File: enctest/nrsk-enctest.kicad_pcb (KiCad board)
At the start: 2 copper layers, 69.6 x 32 mm, 10 parts, among them J1 RP2040-Zero left, J2 RP2040-Zero right, SW1 Layer 1

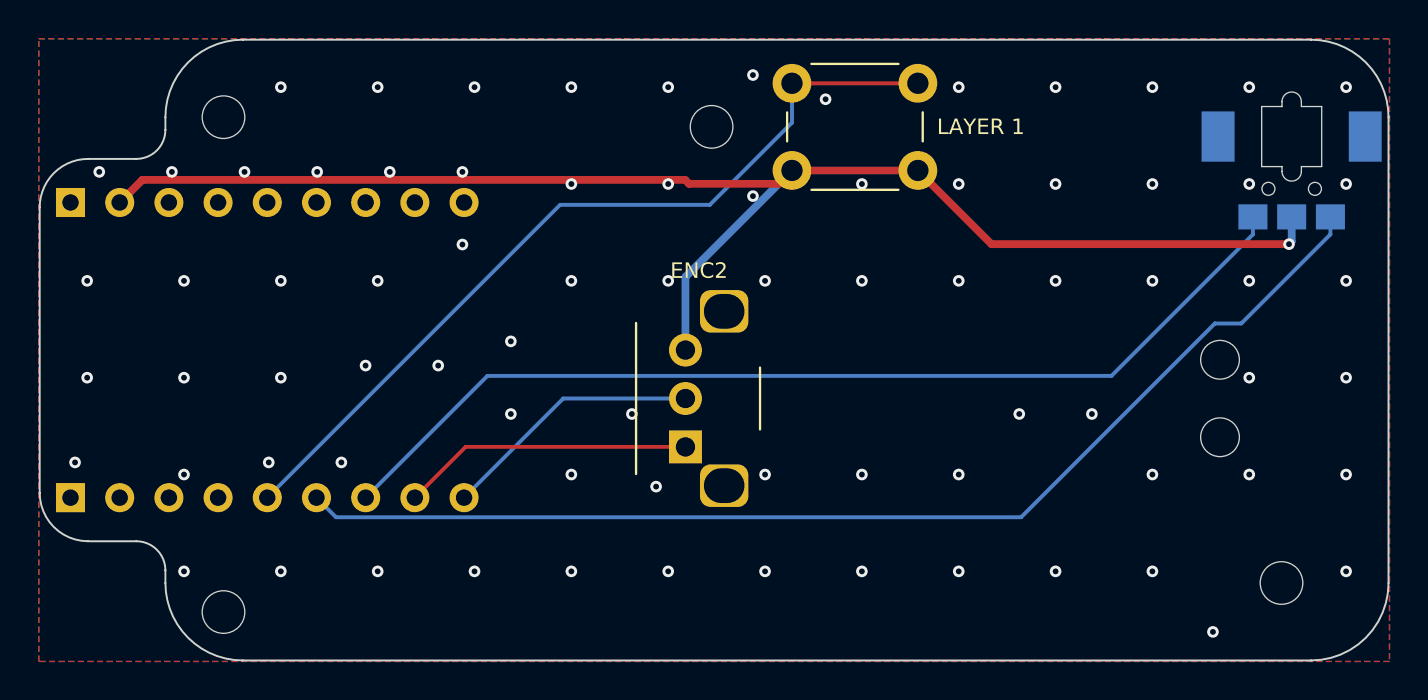
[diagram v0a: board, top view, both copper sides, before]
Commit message: Encoder test board: left M2 holes on the corners' arc centres
The lower-left hole sat 1.5 mm below the F12 row, 2.2 mm from the rounded
corner (drill wall 1.1 mm): an M2 head or hex standoff would overhang the
edge. Both left holes now sit on the corner arcs' centres, 4.0 mm from the
edges and the corner like the others; the lower one is 3.0 mm below the
RP2040-Zero, clear of its boss. Board, fab files, case parts and the
render regenerated (DRC/ERC 0, case checks ok).

Co-Authored-By: Claude Opus 5.5 <noreply@anthropic.com>
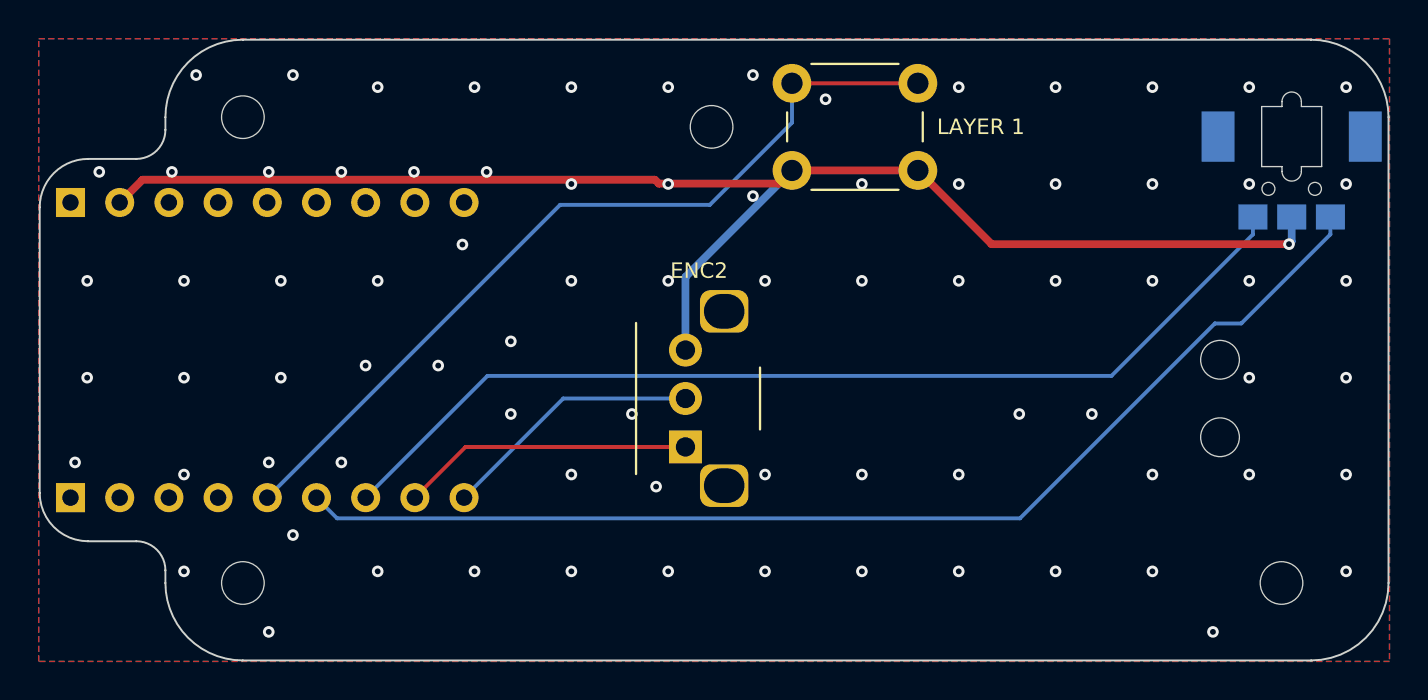
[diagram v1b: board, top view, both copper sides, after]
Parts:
- moved H3 1.80 mm to (148.4, 49.0)
- moved H1 1.00 mm to (148.4, 25.0)
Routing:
- net GND: vias 79 -> 81

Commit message: Encoder test board: hand-rerouted wheel traces, gerbers re-exported
The thumbwheel encoder's tracks were rerouted by hand in KiCad and the GND
zones refilled; DRC is clean (0 violations, 0 unconnected, 0 parity issues).
The gerber zip is re-exported with the same layers and drill options as
build_enctest.sh. Running build_enctest.sh again regenerates the board and
overwrites this routing.

The .kicad_pro changes are KiCad 10 adding its new default ERC settings on save.
KiCad's local .history/ backups are now ignored.

Co-Authored-By: Claude Opus 5.5 <noreply@anthropic.com>
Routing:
- net /WHEEL_A: track 59.8 -> 63.8 mm
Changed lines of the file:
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@@
 			)
 		)
+		(property ki_fp_filters "RotaryEncoder*")
 		(sheetname "/")
 		(sheetfile "nrsk-enctest.kicad_sch")
+		(units
+			(unit
+				(name "A")
+				(pins "A" "C" "B")
+			)
+		)
 		(attr through_hole)
 		(duplicate_pad_numbers_are_jumpers no)
@@
 			(remove_unused_layers no)
 			(net "/DRUM_A")
+			(pinfunction "A_A")
+			(pintype "passive")
 		)
 		(pad "B" thru_hole circle
@@
 			(remove_unused_layers no)
 			(net "/DRUM_B")
+			(pinfunction "B_B")
+			(pintype "passive")
 		)
 		(pad "C" thru_hole circle
@@
 			(remove_unused_layers no)
 			(net "GND")
+			(pinfunction "C_C")
+			(pintype "passive")
 		)
 		(embedded_fonts no)
@@
 		(sheetname "/")
 		(sheetfile "nrsk-enctest.kicad_sch")
+		(units
+			(unit
+				(name "A")
+				(pins "1" "2")
+			)
+		)
 		(attr through_hole)
 		(duplicate_pad_numbers_are_jumpers no)
@@
 			(remove_unused_layers no)
 			(net "/KEY")
+			(pinfunction "1_1")
+			(pintype "passive")
 		)
 		(pad "1" thru_hole circle
@@
 			(remove_unused_layers no)
 			(net "/KEY")
+			(pinfunction "1_1")
+			(pintype "passive")
 		)
 		(pad "2" thru_hole circle
@@
 			(remove_unused_layers no)
 			(net "GND")
+			(pinfunction "2_2")
+			(pintype "passive")
 		)
 		(pad "2" thru_hole circle
@@
 			(remove_unused_layers no)
 			(net "GND")
+			(pinfunction "2_2")
+			(pintype "passive")
 		)
 		(embedded_fonts no)
@@
 			)
 		)
+		(property ki_fp_filters "Connector*:*_1x??_*")
 		(sheetname "/")
 		(sheetfile "nrsk-enctest.kicad_sch")
+		(units
+			(unit
+				(name "A")
+				(pins "1" "2" "3" "4" "5" "6" "7" "8" "9")
+			)
+		)
 		(attr through_hole)
 		(duplicate_pad_numbers_are_jumpers no)
@@
 			(remove_unused_layers no)
 			(net "unconnected-(J1-Pin_1-Pad1)")
+			(pinfunction "Pin_1_1")
+			(pintype "passive+no_connect")
 		)
 		(pad "2" thru_hole circle
@@
 			(remove_unused_layers no)
 			(net "GND")
+			(pinfunction "Pin_2_2")
+			(pintype "passive")
 		)
 		(pad "3" thru_hole circle
@@
 			(remove_unused_layers no)
 			(net "unconnected-(J1-Pin_3-Pad3)")
+			(pinfunction "Pin_3_3")
+			(pintype "passive+no_connect")
 		)
 		(pad "4" thru_hole circle
@@
 			(remove_unused_layers no)
 			(net "unconnected-(J1-Pin_4-Pad4)")
+			(pinfunction "Pin_4_4")
+			(pintype "passive+no_connect")
 		)
 		(pad "5" thru_hole circle
@@
 			(remove_unused_layers no)
 			(net "unconnected-(J1-Pin_5-Pad5)")
+			(pinfunction "Pin_5_5")
+			(pintype "passive+no_connect")
 		)
 		(pad "6" thru_hole circle
@@
 			(remove_unused_layers no)
 			(net "unconnected-(J1-Pin_6-Pad6)")
+			(pinfunction "Pin_6_6")
+			(pintype "passive+no_connect")
 		)
 		(pad "7" thru_hole circle
@@
 			(remove_unused_layers no)
 			(net "unconnected-(J1-Pin_7-Pad7)")
+			(pinfunction "Pin_7_7")
+			(pintype "passive+no_connect")
 		)
 		(pad "8" thru_hole circle
@@
 			(remove_unused_layers no)
 			(net "unconnected-(J1-Pin_8-Pad8)")
+			(pinfunction "Pin_8_8")
+			(pintype "passive+no_connect")
 		)
 		(pad "9" thru_hole circle
@@
 			(remove_unused_layers no)
 			(net "unconnected-(J1-Pin_9-Pad9)")
+			(pinfunction "Pin_9_9")
+			(pintype "passive+no_connect")
 		)
 		(embedded_fonts no)
@@
 			)
 		)
+		(property ki_fp_filters "Connector*:*_1x??_*")
 		(sheetname "/")
 		(sheetfile "nrsk-enctest.kicad_sch")
+		(units
+			(unit
+				(name "A")
+				(pins "1" "2" "3" "4" "5" "6" "7" "8" "9")
+			)
+		)
 		(attr through_hole)
 		(duplicate_pad_numbers_are_jumpers no)
@@
 			(remove_unused_layers no)
 			(net "unconnected-(J2-Pin_1-Pad1)")
+			(pinfunction "Pin_1_1")
+			(pintype "passive+no_connect")
 		)
 		(pad "2" thru_hole circle
@@
 			(remove_unused_layers no)
 			(net "unconnected-(J2-Pin_2-Pad2)")
+			(pinfunction "Pin_2_2")
+			(pintype "passive+no_connect")
 		)
 		(pad "3" thru_hole circle
@@
 			(remove_unused_layers no)
 			(net "unconnected-(J2-Pin_3-Pad3)")
+			(pinfunction "Pin_3_3")
+			(pintype "passive+no_connect")
 		)
 		(pad "4" thru_hole circle
@@
 			(remove_unused_layers no)
 			(net "unconnected-(J2-Pin_4-Pad4)")
+			(pinfunction "Pin_4_4")
+			(pintype "passive+no_connect")
 		)
 		(pad "5" thru_hole circle
@@
 			(remove_unused_layers no)
 			(net "/KEY")
+			(pinfunction "Pin_5_5")
+			(pintype "passive")
 		)
 		(pad "6" thru_hole circle
@@
 			(remove_unused_layers no)
 			(net "/WHEEL_A")
+			(pinfunction "Pin_6_6")
+			(pintype "passive")
 		)
 		(pad "7" thru_hole circle
@@
 			(remove_unused_layers no)
 			(net "/WHEEL_B")
+			(pinfunction "Pin_7_7")
+			(pintype "passive")
 		)
 		(pad "8" thru_hole circle
@@
 			(remove_unused_layers no)
 			(net "/DRUM_A")
+			(pinfunction "Pin_8_8")
+			(pintype "passive")
 		)
 		(pad "9" thru_hole circle
@@
 			(remove_unused_layers no)
 			(net "/DRUM_B")
+			(pinfunction "Pin_9_9")
+			(pintype "passive")
 		)
 		(embedded_fonts no)
@@
 			)
 		)
+		(property ki_fp_filters "RotaryEncoder*")
 		(sheetname "/")
 		(sheetfile "nrsk-enctest.kicad_sch")
+		(units
+			(unit
+				(name "A")
+				(pins "A" "C" "B")
+			)
+		)
 		(attr smd)
 		(duplicate_pad_numbers_are_jumpers no)
@@
 			(layers "B.Cu" "B.Mask" "B.Paste")
 			(net "/WHEEL_A")
+			(pinfunction "A_A")
+			(pintype "passive")
 		)
 		(pad "B" smd rect
@@
 			(layers "B.Cu" "B.Mask" "B.Paste")
 			(net "/WHEEL_B")
+			(pinfunction "B_B")
+			(pintype "passive")
 		)
 		(pad "C" smd rect
@@
 			(layers "B.Cu" "B.Mask" "B.Paste")
 			(net "GND")
+			(pinfunction "C_C")
+			(pintype "passive")
 		)
 		(embedded_fonts no)
@@
 	)
 	(segment
-		(start 198.5592 35.6502)
-		(end 188.497 45.7124)
-		(width 0.2)
-		(layer "B.Cu")
-		(net "/WHEEL_A")
-	)
-	(segment
-		(start 188.497 45.7124)
+		(start 196.7876 45.7124)
 		(end 153.2424 45.7124)
 		(width 0.2)
@@
 	)
 	(segment
-		(start 204.525 31.0517)
-		(end 199.9265 35.6502)
+		(start 204.525 30.15)
+		(end 204.525 37.975)
 		(width 0.2)
 		(layer "B.Cu")
@@
 	)
 	(segment
-		(start 204.525 30.15)
-		(end 204.525 31.0517)
+		(start 204.525 37.975)
+		(end 196.7876 45.7124)
 		(width 0.2)
 		(layer "B.Cu")
-		(net "/WHEEL_A")
-	)
-	(segment
-		(start 199.9265 35.6502)
-		(end 198.5592 35.6502)
-		(width 0.2)
-		(layer "B.Cu")

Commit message: Encoder test board: drop the GND stitching via at the top-left edge
The stitching via between the RP2040-Zero header's pins 1 and 2 had only
0.37 mm of copper to the board edge (DRC minimum 0.3 mm), too tight for the
outline routing tolerance. GND keeps plenty of other vias. Zones refilled,
DRC clean, gerbers re-exported.

Co-Authored-By: Claude Opus 5.5 <noreply@anthropic.com>
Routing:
- net GND: vias 81 -> 80
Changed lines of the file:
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@@
-	)
-	(via
-		(at 140.96 27.825)
-		(size 0.6)
-		(drill 0.3)
-		(layers "F.Cu" "B.Cu")
-		(net "GND")
 	)
 	(via

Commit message: Encoder test board: drop the GND stitching via by the top edge
The via at (145.96, 22.82) had 0.45 mm of copper to the top edge. The
closest via to the outline is now 0.66 mm. Zones refilled, DRC clean,
gerbers re-exported.

Co-Authored-By: Claude Opus 5.5 <noreply@anthropic.com>
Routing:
- net GND: vias 80 -> 79
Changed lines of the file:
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@@
-	)
-	(via
-		(at 145.96 22.825)
-		(size 0.6)
-		(drill 0.3)
-		(layers "F.Cu" "B.Cu")
-		(net "GND")
 	)
 	(via

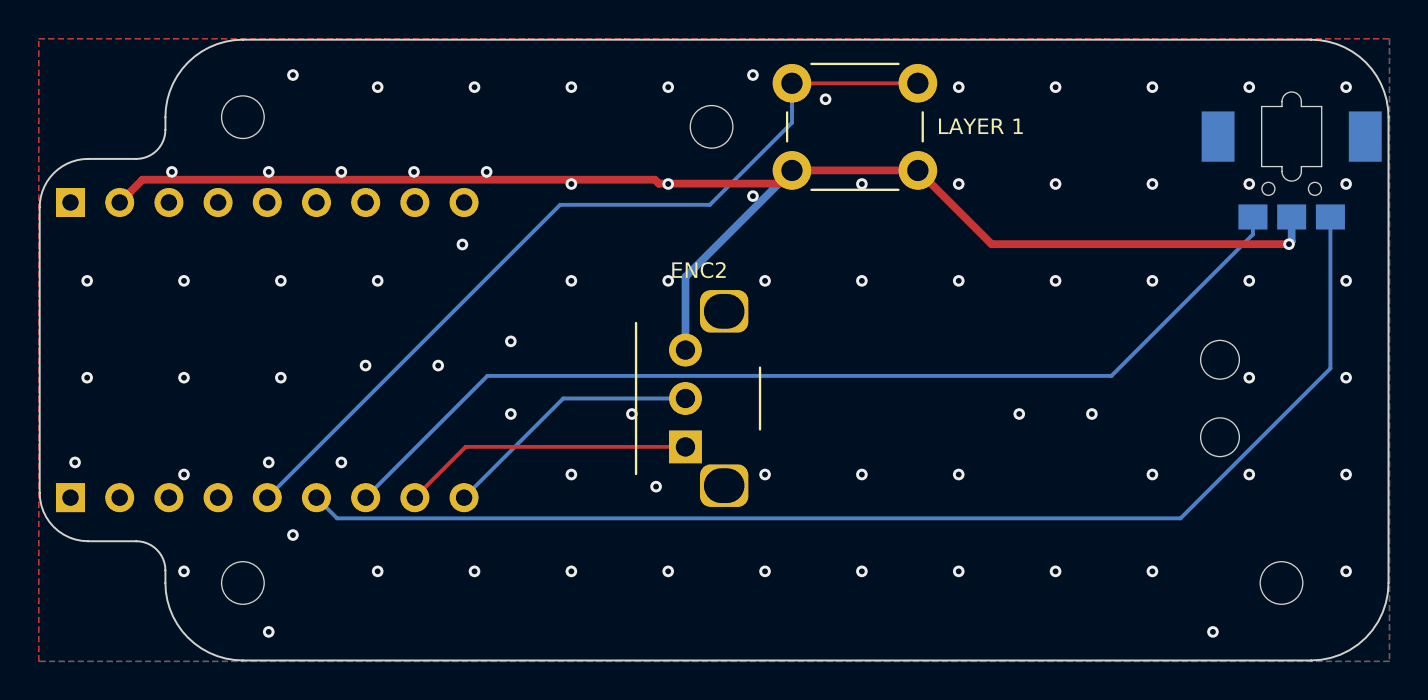
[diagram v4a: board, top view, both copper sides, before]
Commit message: Encoder test board: wider MCU tongue, hand route kept, stitching vias off the edge
- The tongue under the RP2040-Zero is 0.5 mm wider on each side (TONGUE_HW +2.75),
  so the pin pads and the GND copper round them sit well inside the outline. The
  case's tunnel follows it (case checks pass).
- WHEEL_A as routed by hand is now placed by make_enctest.py as locked tracks, so
  build_enctest.sh keeps it; Freerouting routes the rest round it.
- route.py keeps a stitching via's copper STITCH_EDGE (1.0 mm) from the board edge.
  This also applies to the keyboard halves on their next build.

Rebuilt with build_enctest.sh: DRC 0 violations / 0 unconnected / 0 parity; the
closest via to the edge is now 1.175 mm (was 0.37 mm).

Co-Authored-By: Claude Opus 5.5 <noreply@anthropic.com>
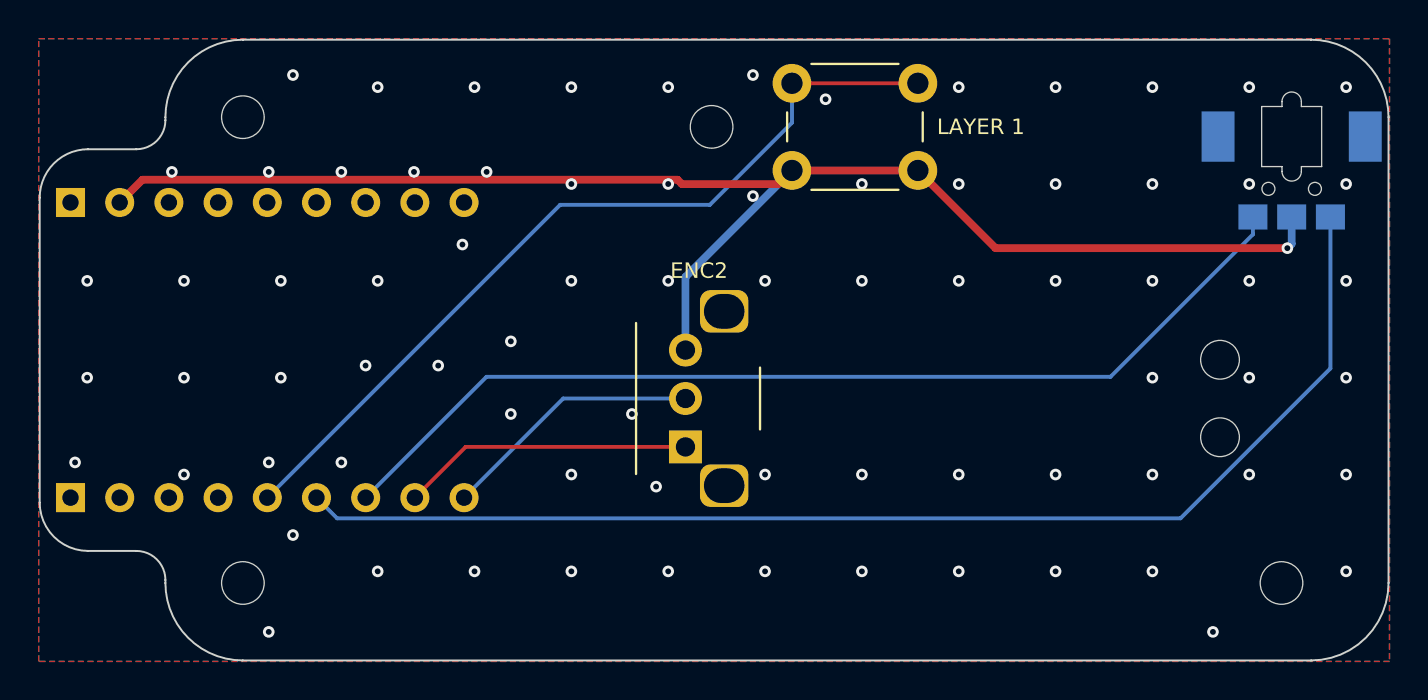
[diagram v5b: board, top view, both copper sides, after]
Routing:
- net GND: track 75.8 -> 76.1 mm, vias 79 -> 78
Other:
- outline, holes or cut-outs redrawn

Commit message: Encoder test board: front GND trace rerouted by hand, wheel and back pour locked
The F.Cu GND trace from the RP2040-Zero now drops to y = 31 and runs along there
before turning up 45 degrees to the switch, instead of the old run at y = 28.2.
The thumbwheel encoder footprint and the B.Cu GND zone are locked, like the
hand-routed WHEEL_A. DRC is clean; gerbers re-exported from this board.

Co-Authored-By: Claude Opus 5.5 <noreply@anthropic.com>
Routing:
- net GND: track 76.1 -> 77.2 mm
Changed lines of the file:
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@@
 	)
 	(footprint "nrsk:Alps_EC05E1220401"
+		(locked yes)
 		(layer "B.Cu")
 		(at 202.525 26 180)
@@
 	)
 	(segment
-		(start 143.1909 28.2291)
-		(end 170.8146 28.2291)
+		(start 142.015 29.405)
+		(end 143.61 31)
 		(width 0.4)
 		(layer "F.Cu")
@@
 	)
 	(segment
+		(start 143.61 31)
+		(end 173.5 31)
+		(width 0.4)
+		(layer "F.Cu")
+		(net "GND")
+	)
+	(segment
+		(start 173.5 31)
+		(end 176 28.5)
+		(width 0.4)
+		(layer "F.Cu")
+		(net "GND")
+	)
+	(segment
 		(start 176.725 27.75)
 		(end 183.225 27.75)
-		(width 0.4)
-		(layer "F.Cu")
-		(net "GND")
-	)
-	(segment
-		(start 171.0369 28.4514)
-		(end 176.0236 28.4514)
-		(width 0.4)
-		(layer "F.Cu")
-		(net "GND")
-	)
-	(segment
-		(start 142.015 29.405)
-		(end 143.1909 28.2291)
-		(width 0.4)
-		(layer "F.Cu")
-		(net "GND")
-	)
-	(segment
-		(start 170.8146 28.2291)
-		(end 171.0369 28.4514)
 		(width 0.4)
 		(layer "F.Cu")
@@
 	(zone
 		(net "GND")
+		(locked yes)
 		(layer "B.Cu")
 		(name "GND")
